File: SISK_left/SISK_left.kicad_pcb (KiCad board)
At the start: 2 copper layers, 142.1 x 121.8 mm, 68 parts, among them J1 OLED_128x32, J2 Battery Socket, SW1 "Esc", SW10 "E", SW11 "R", SW12 "T", SW13 "Caps Lock", SW14 "A", SW15 "S", SW16 "D", SW17 "F", SW18 "G", SW19 "Left Shift", SW2 "1", SW20 ">", SW21 "Y", SW22 "X", SW23 "C", SW24 "V", SW25 "B", SW26 "Ctrl", SW27 "Super", SW28 "Alt", SW29 "FN", SW3 "2", SW30 "Space", SW31 SW_SPDT, SW4 "3", SW5 "4", SW6 "5", SW7 "Tab", SW8 "Q", SW9 "W", U1 Nice_Nano_V2

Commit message: up
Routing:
- net COL4: track 148.5 -> 150.3 mm
- net ROW0: track 191.7 -> 192.6 mm
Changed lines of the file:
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@@
 		)
 		(fp_text user "GND"
-			(at -6.35 5.461 360)
+			(at -6.35 5.461 0)
 			(layer "B.SilkS")
 			(hide yes)
@@
 		)
 		(fp_text user "D7"
-			(at 6.35 5.461 360)
+			(at 6.35 5.461 0)
 			(layer "B.SilkS")
 			(hide yes)
@@
 		(at 241.545 216.72)
 		(property "Reference" "J1"
-			(at 7.75 10 360)
+			(at 7.75 10 0)
 			(layer "F.SilkS")
 			(hide yes)
@@
 		)
 		(property "Value" "OLED_128x32"
-			(at 5.75 5.75 360)
+			(at 5.75 5.75 0)
 			(layer "F.Fab")
 			(effects
@@
 		)
 		(property "Footprint" "ScottoKeebs_Components:OLED_128x32"
-			(at 0 0 360)
+			(at 0 0 0)
 			(layer "F.Fab")
 			(hide yes)
@@
 		)
 		(property "Datasheet" ""
-			(at 0 0 360)
+			(at 0 0 0)
 			(layer "F.Fab")
 			(hide yes)
@@
 		)
 		(property "Description" ""
-			(at 0 0 360)
+			(at 0 0 0)
 			(layer "F.Fab")
 			(hide yes)
@@
 	)
 	(segment
+		(start 247.72625 250.395)
+		(end 264.51375 250.395)
+		(width 0.25)
+		(layer "B.Cu")
+		(net 4)
+	)
+	(segment
 		(start 186.529375 248.629375)
 		(end 189.295 251.395)
@@
 	)
 	(segment
+		(start 264.51375 250.395)
+		(end 265.645 251.52625)
+		(width 0.25)
+		(layer "B.Cu")
+		(net 4)
+	)
+	(segment
 		(start 246.595 251.52625)
 		(end 227.545 251.52625)
@@
 	)
 	(segment
-		(start 175.345 251.52625)
-		(end 178.26375 251.52625)
+		(start 246.595 251.52625)
+		(end 247.72625 250.395)
 		(width 0.25)
 		(layer "B.Cu")
@@
 	)
 	(segment
-		(start 171.27625 251.52625)
-		(end 171.145 251.395)
+		(start 175.345 251.52625)
+		(end 178.26375 251.52625)
 		(width 0.25)
 		(layer "B.Cu")
@@
 	)
 	(segment
-		(start 246.595 251.52625)
-		(end 265.645 251.52625)
+		(start 171.27625 251.52625)
+		(end 171.145 251.395)
 		(width 0.25)
 		(layer "B.Cu")
@@
 	)
 	(segment
-		(start 253.945 293.345)
-		(end 255.395 294.795)
+		(start 252.345 289.945)
+		(end 252.345 291.745)
+		(width 0.25)
+		(layer "F.Cu")
+		(net 42)
+	)
+	(segment
+		(start 274.98 318.18)
+		(end 278.01625 318.18)
+		(width 0.25)
+		(layer "F.Cu")
+		(net 42)
+	)
+	(segment
+		(start 256.87 293.32)
+		(end 259.12 293.32)
 		(width 0.25)
 		(layer "F.Cu")
@@
 	)
 	(segment
+		(start 259.12 293.32)
+		(end 263.745 297.945)
+		(width 0.25)
+		(layer "F.Cu")
+		(net 42)
+	)
+	(segment
+		(start 255.595 276.795)
+		(end 253.945 278.445)
+		(width 0.25)
+		(layer "F.Cu")
+		(net 42)
+	)
+	(segment
 		(start 251.8225 298.3675)
 		(end 251.8225 299.13)
@@
 	)
 	(segment
-		(start 256.245 293.945)
-		(end 259.745 293.945)
+		(start 255.395 294.795)
+		(end 256.87 293.32)
 		(width 0.25)
 		(layer "F.Cu")
@@
 	)
 	(segment
-		(start 255.595 276.795)
-		(end 253.945 278.445)
+		(start 253.945 288.345)
+		(end 252.345 289.945)
 		(width 0.25)
 		(layer "F.Cu")
@@
 	)
 	(segment
-		(start 253.945 278.445)
-		(end 253.945 293.345)
+		(start 263.745 297.945)
+		(end 263.745 306.945)
 		(width 0.25)
 		(layer "F.Cu")
@@
 	)
 	(segment
-		(start 255.595 294.595)
-		(end 256.245 293.945)
-		(width 0.25)
-		(layer "F.Cu")
-		(net 42)
-	)
-	(segment
 		(start 244.91 241.98)
 		(end 243.645 243.245)
@@
 	)
 	(segment
-		(start 255.595 294.595)
-		(end 255.395 294.795)
+		(start 253.945 278.445)
+		(end 253.945 288.345)
 		(width 0.25)
 		(layer "F.Cu")
@@
 	)
 	(segment
+		(start 252.345 291.745)
+		(end 255.395 294.795)
+		(width 0.25)
+		(layer "F.Cu")
+		(net 42)
+	)
+	(segment
 		(start 255.645 257.045)
 		(end 255.6325 257.0325)
@@
 	)
 	(segment
-		(start 263.745 298.045)
-		(end 263.745 306.945)
-		(width 0.25)
-		(layer "F.Cu")
-		(net 42)
-	)
-	(segment
 		(start 258.745 233.27)
 		(end 259.91 232.105)
@@
 	)
 	(segment
-		(start 263.745 297.945)
-		(end 263.745 298.045)
-		(width 0.25)
-		(layer "F.Cu")
-		(net 42)
-	)
-	(segment
 		(start 243.645 247.345)
 		(end 252.645 256.345)
@@
 	)
 	(segment
-		(start 259.745 293.945)
-		(end 263.745 297.945)
-		(width 0.25)
-		(layer "F.Cu")
-		(net 42)
-	)
-	(segment
 		(start 255.6325 251.66375)
 		(end 258.745 248.55125)
@@
 		(width 0.25)
 		(layer "F.Cu")
-		(net 42)
-	)
-	(segment
-		(start 274.98 318.18)
-		(end 278.01625 318.18)
-		(width 0.25)
-		(layer "F.Cu")

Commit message: changes after first review
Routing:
- net COL3: track 149.9 -> 165.1 mm
- net COL5: track 111.3 -> 118.1 mm
- net COL4: track 150.3 -> 145.9 mm
- net COL2: track 155.2 -> 159.3 mm
- net Net-(D4-A): track 20.0 -> 22.8 mm
- net ROW3: track 229.3 -> 228.2 mm
- net Net-(D13-A): track 19.9 -> 20.6 mm
- net Net-(D14-A): track 19.9 -> 20.6 mm
- net Net-(D21-A): track 20.1 -> 20.8 mm
- net ROW1: track 227.9 -> 228.6 mm
- net Net-(J1-VCC): track 34.1 -> 33.4 mm
- net Net-(D30-A): track 20.1 -> 20.7 mm
- net Net-(D29-A): track 20.2 -> 20.9 mm
- net Net-(D20-A): track 19.9 -> 20.5 mm
- net Net-(D8-A): track 20.2 -> 20.8 mm
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
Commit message: changed nice nano footprint
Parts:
- U1: footprint ScottoKeebs_MCU:Arduino_Pro_Micro -> nice-nano-kicad-master:nice_nano
- turned U1 to 180 degrees
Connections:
- SW31 pad 3: unconnected-(SW31-C-Pad3) -> GND
- SW31 pad MP: (no net) -> GND
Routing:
- net ROW3: track 228.2 -> 229.8 mm
- net ROW2: track 183.9 -> 185.1 mm
- net ROW1: track 228.6 -> 229.7 mm
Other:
- board text added: "009"
- board text added: "106"

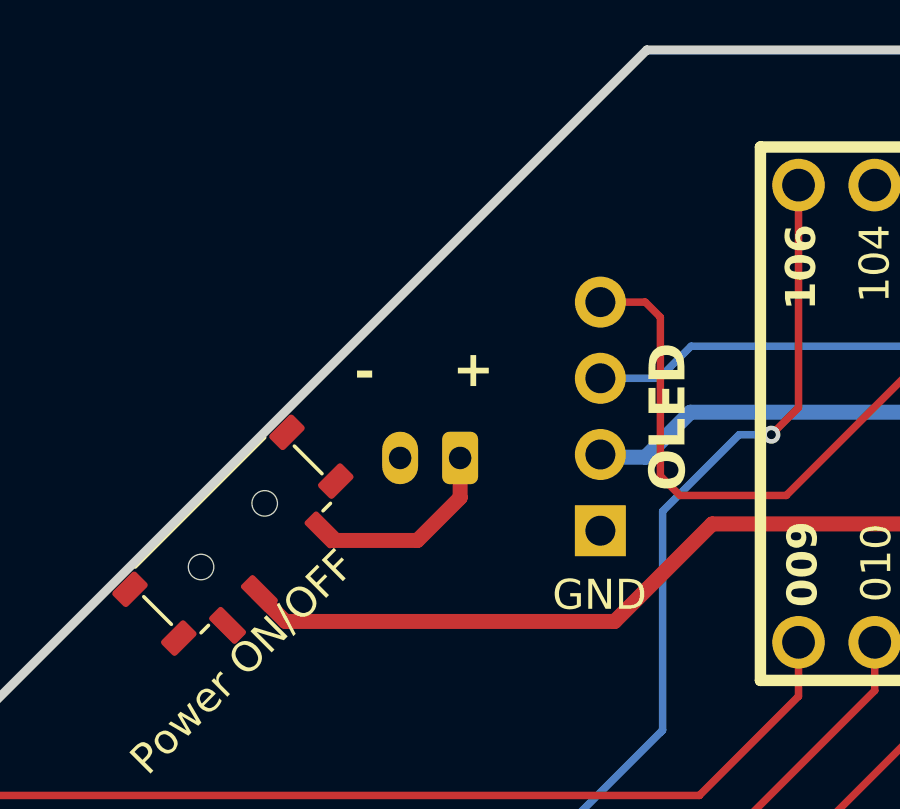
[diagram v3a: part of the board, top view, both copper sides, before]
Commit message: added some text and alternative header for Power Switch
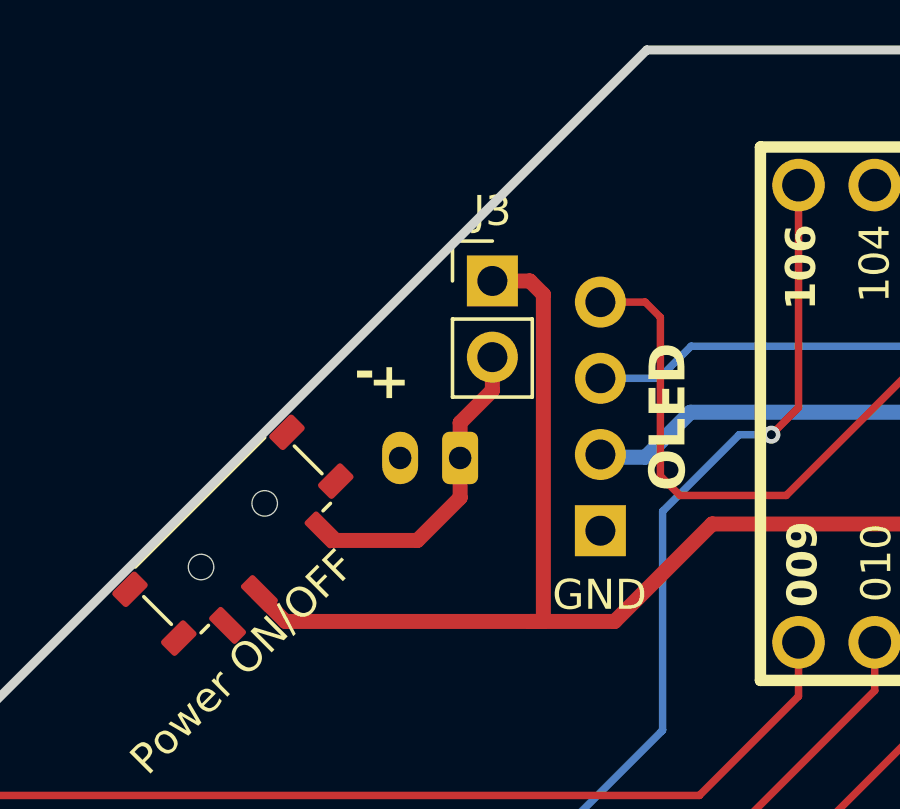
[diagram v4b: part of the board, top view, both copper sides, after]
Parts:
- added J3: alternative ON/OFF SW(wired), Connector_PinHeader_2.54mm:PinHeader_1x02_P2.54mm_Vertical, F.Cu at (239.5, 218.2)
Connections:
- SW31 pad 3: GND -> unconnected-(SW31-C-Pad3)
- SW31 pad MP: GND -> (no net)
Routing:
- net Net-(J3-Pin_1): track 50.3 -> 63.6 mm
- net Net-(J2-Pin_1): track 6.77 -> 10.6 mm
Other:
- board text added: "designed by d4ve October 2024 Rev 1.0"

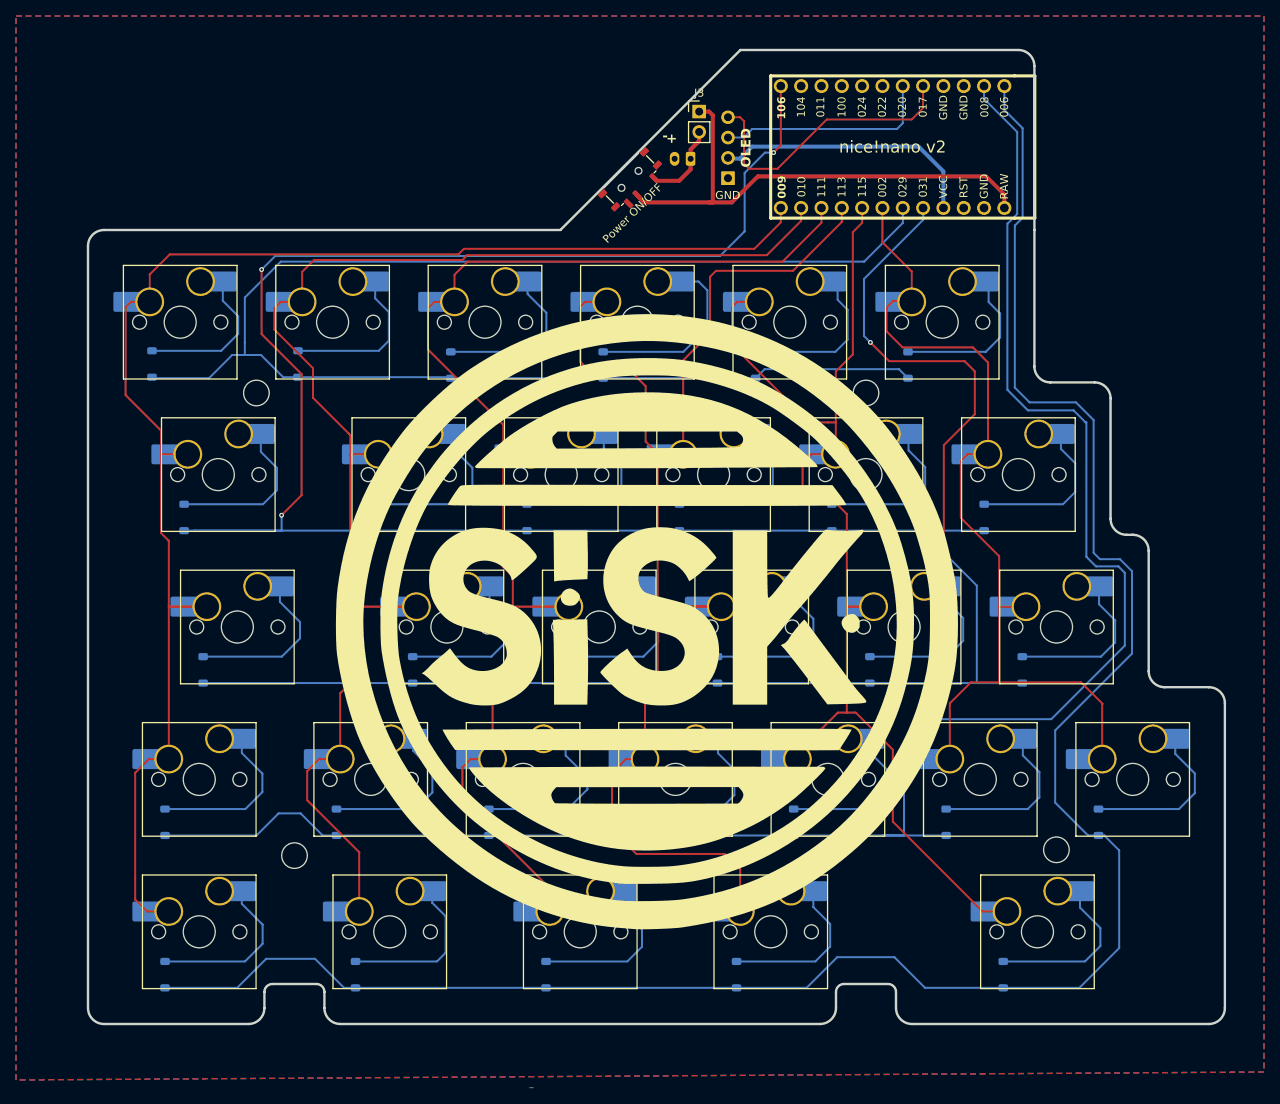
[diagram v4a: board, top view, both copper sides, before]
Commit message: changed file structure, added new project for 60%, changed main footprints for hotswap sockets
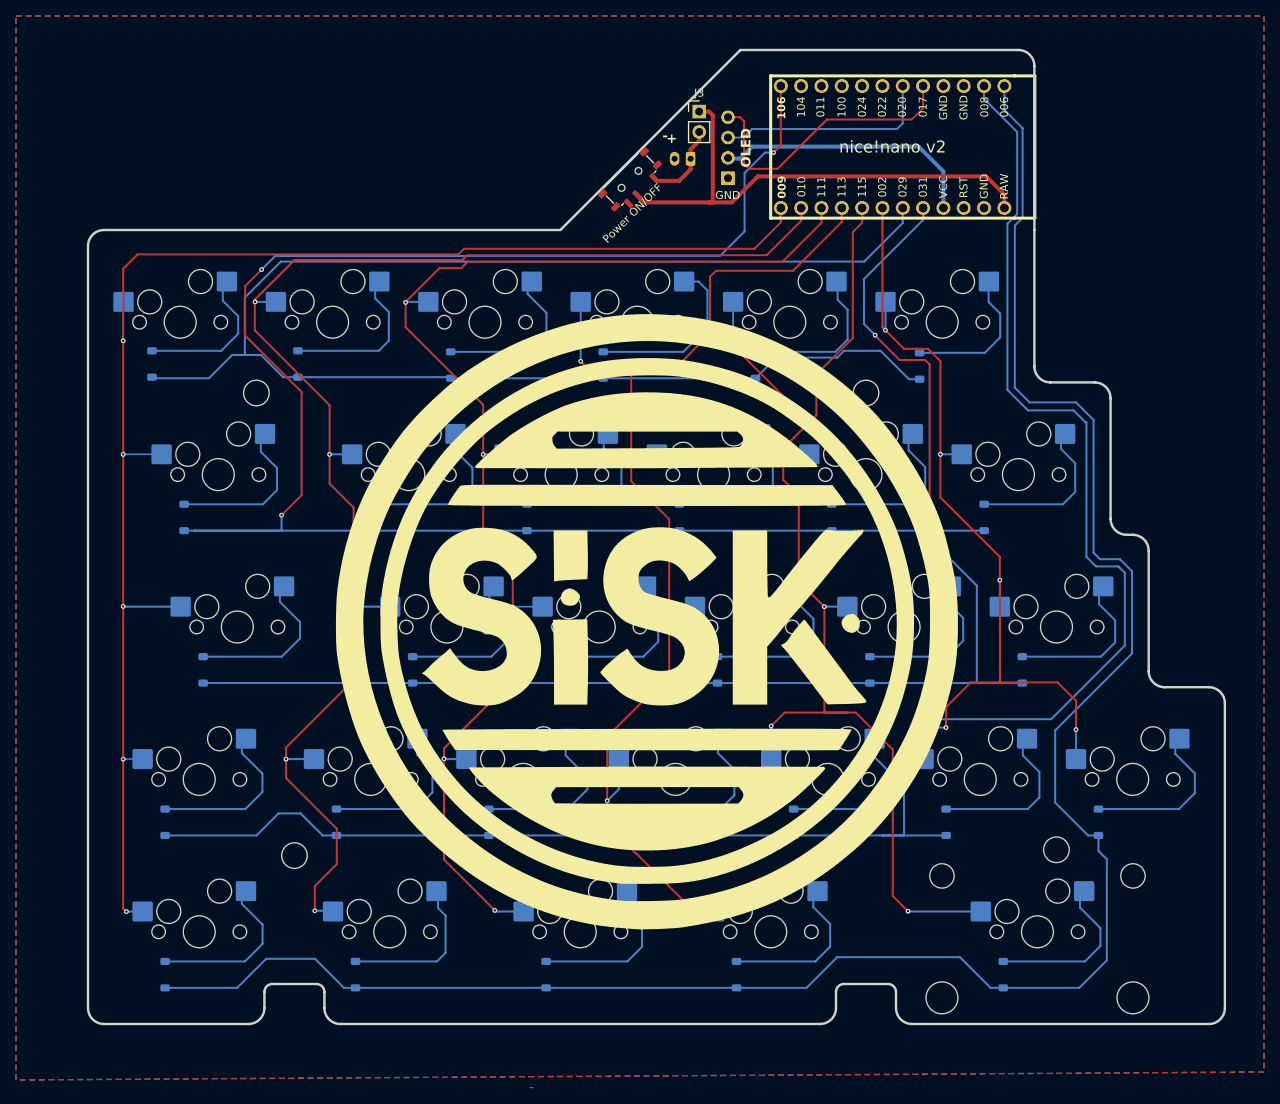
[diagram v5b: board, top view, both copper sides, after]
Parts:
- SW1, SW10, SW11, SW12, SW14, SW15, SW16, SW17, SW18, SW2, SW20, SW21, SW22, SW23, SW24, SW25, SW3, SW4, SW5, SW6, SW8, SW9: footprint ScottoKeebs_Hotswap:Hotswap_MX_Plated_1.00u -> MX_Hotswap:MX-Hotswap-1U; moved to B.Cu
- SW13: footprint ScottoKeebs_Hotswap:Hotswap_MX_Plated_1.75u -> MX_Hotswap:MX-Hotswap-1.75U; moved to B.Cu
- SW19, SW26, SW27, SW28, SW29: footprint ScottoKeebs_Hotswap:Hotswap_MX_Plated_1.25u -> MX_Hotswap:MX-Hotswap-1.25U; moved to B.Cu
- SW30: footprint ScottoKeebs_Hotswap:Hotswap_MX_Plated_2.25u -> MX_Hotswap:MX-Hotswap-2.25U; moved to B.Cu
- SW7: footprint ScottoKeebs_Hotswap:Hotswap_MX_Plated_1.50u -> MX_Hotswap:MX-Hotswap-1.5U; moved to B.Cu
- moved D6 1.45 mm to (267.1, 250.0)
- turned SW1 to 180 degrees
- turned SW10 to 180 degrees
- turned SW11 to 180 degrees
- turned SW12 to 180 degrees
- turned SW13 to 180 degrees
- turned SW14 to 180 degrees
- turned SW15 to 180 degrees
- turned SW16 to 180 degrees
- turned SW17 to 180 degrees
- turned SW18 to 180 degrees
- turned SW19 to 180 degrees
- turned SW2 to 180 degrees
- turned SW20 to 180 degrees
- turned SW21 to 180 degrees
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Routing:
- net COL3: track 165.1 -> 146.2 mm, vias 0 -> 5
- net COL5: track 118.1 -> 111.0 mm, vias 0 -> 5
- net ROW2: track 185.1 -> 178.3 mm
- net COL1: track 172.8 -> 178.8 mm, vias 0 -> 5
- net COL0: track 182.5 -> 188.3 mm, vias 0 -> 5
- net COL4: track 145.9 -> 149.5 mm, vias 0 -> 5
- net ROW0: track 193.1 -> 196.5 mm
- net COL2: track 159.3 -> 161.9 mm, vias 0 -> 5
- net ROW4: track 256.0 -> 254.3 mm
- net ROW1: track 229.7 -> 231.4 mm
- net Net-(D6-A): track 20.1 -> 18.7 mm

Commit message: fixed schematics, added optional pullup resistors
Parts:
- added R1: 5K, Resistor_SMD:R_1206_3216Metric_Pad1.30x1.75mm_HandSolder, B.Cu at (229.5, 232.4)
- added R2: 5K, Resistor_SMD:R_1206_3216Metric_Pad1.30x1.75mm_HandSolder, B.Cu at (232.1, 232.4)
- D1, D10, D11, D12, D13, D14, D15, D16, D17, D18, D19, D2, D20, D21, D22, D23, D24, D25, D26, D27, D28, D29, D3, D30, D4, D5, D6, D7, D8, D9: value D -> 1n4148
- J2: value Battery Socket -> BAT
- J3: value alternative ON/OFF SW(wired) -> CONN_ALT
- SW1: value "Esc" -> SW_push
- SW10: value "E" -> SW_push
- SW11: value "R" -> SW_push
- SW12: value "T" -> SW_push
- SW13: value "Caps Lock" -> SW_push
- SW14: value "A" -> SW_push
- SW15: value "S" -> SW_push
- SW16: value "D" -> SW_push
- SW17: value "F" -> SW_push
- SW18: value "G" -> SW_push
- SW19: value "Left Shift" -> SW_push
- SW2: value "1" -> SW_push
- SW20: value ">" -> SW_push
- SW21: value "Y" -> SW_push
- SW22: value "X" -> SW_push
- SW23: value "C" -> SW_push
- SW24: value "V" -> SW_push
- SW25: value "B" -> SW_push
- SW26: value "Ctrl" -> SW_push
- SW27: value "Super" -> SW_push
- SW28: value "Alt" -> SW_push
- SW29: value "FN" -> SW_push
- SW3: value "2" -> SW_push
- SW30: value "Space" -> SW_push
- SW4: value "3" -> SW_push
- SW5: value "4" -> SW_push
- SW6: value "5" -> SW_push
- SW7: value "Tab" -> SW_push
- SW8: value "Q" -> SW_push
- SW9: value "W" -> SW_push
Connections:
- net Net-(J1-SCL) renamed /SCL
- net Net-(J1-SDA) renamed /SDA
- net Net-(J1-VCC) renamed /VCC
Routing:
- net /SDA: track 36.1 -> 57.2 mm
- net /VCC: track 33.4 -> 51.6 mm
- net /SCL: track 27.2 -> 43.4 mm
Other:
- board text added: "Bat"

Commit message: fixed some issues
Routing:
- net GND: vias 0 -> 20

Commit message: fixed most of issues, updated 60% version
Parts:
- R1, R2: value 5K -> 2K2
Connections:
- net /VCC renamed +3.3V
- net Net-(J2-Pin_1) renamed +BATT
- net Net-(J3-Pin_1) renamed +VDC
